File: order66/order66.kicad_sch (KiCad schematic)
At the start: 146 parts, among them J1 NICEVIEW, J2 Pouch Battery Connector, J3 swd connector, J6 millmax connector, SW1 AUX1, SW10 Z, SW11 AUX7, SW12 2, SW13 W, SW14 S, SW15 X, SW16 LALT, SW17 3, SW18 E, SW19 D, SW2 ESC, SW20 C, SW21 GUI, SW22 4, SW23 R, SW24 F, SW25 V, SW26 RAISE, SW27 5, SW28 T, SW29 G, SW3 TAB, SW30 B, SW31 LSPACE, SW32 AUX2, SW33 6, SW34 Y, SW35 H, SW36 N, SW37 RSPACE, SW38 AUX3, SW39 7, SW4 CAPSLCK, SW40 U, SW41 J, SW42 M, SW43 LOWER, SW44 AUX4, SW45 8, SW46 I, SW47 K, SW48 ,<, SW49 LEFT, SW5 LSHIFT, SW50 9, SW51 O, SW52 L, SW53 .>, SW54 DOWN, SW55 AUX5, SW56 0, SW57 P, SW58 ;:, SW59 /?, SW6 LCTRL, SW60 UP, SW61 AUX6, SW62 BACKSPACE, SW63 BACKSLACH, SW64 ENTER, SW65 RSHIFT, SW66 RIGHT, SW67 RST, SW68 ON/OFF, SW7 1, SW8 Q, SW9 A, U1 NiceNano

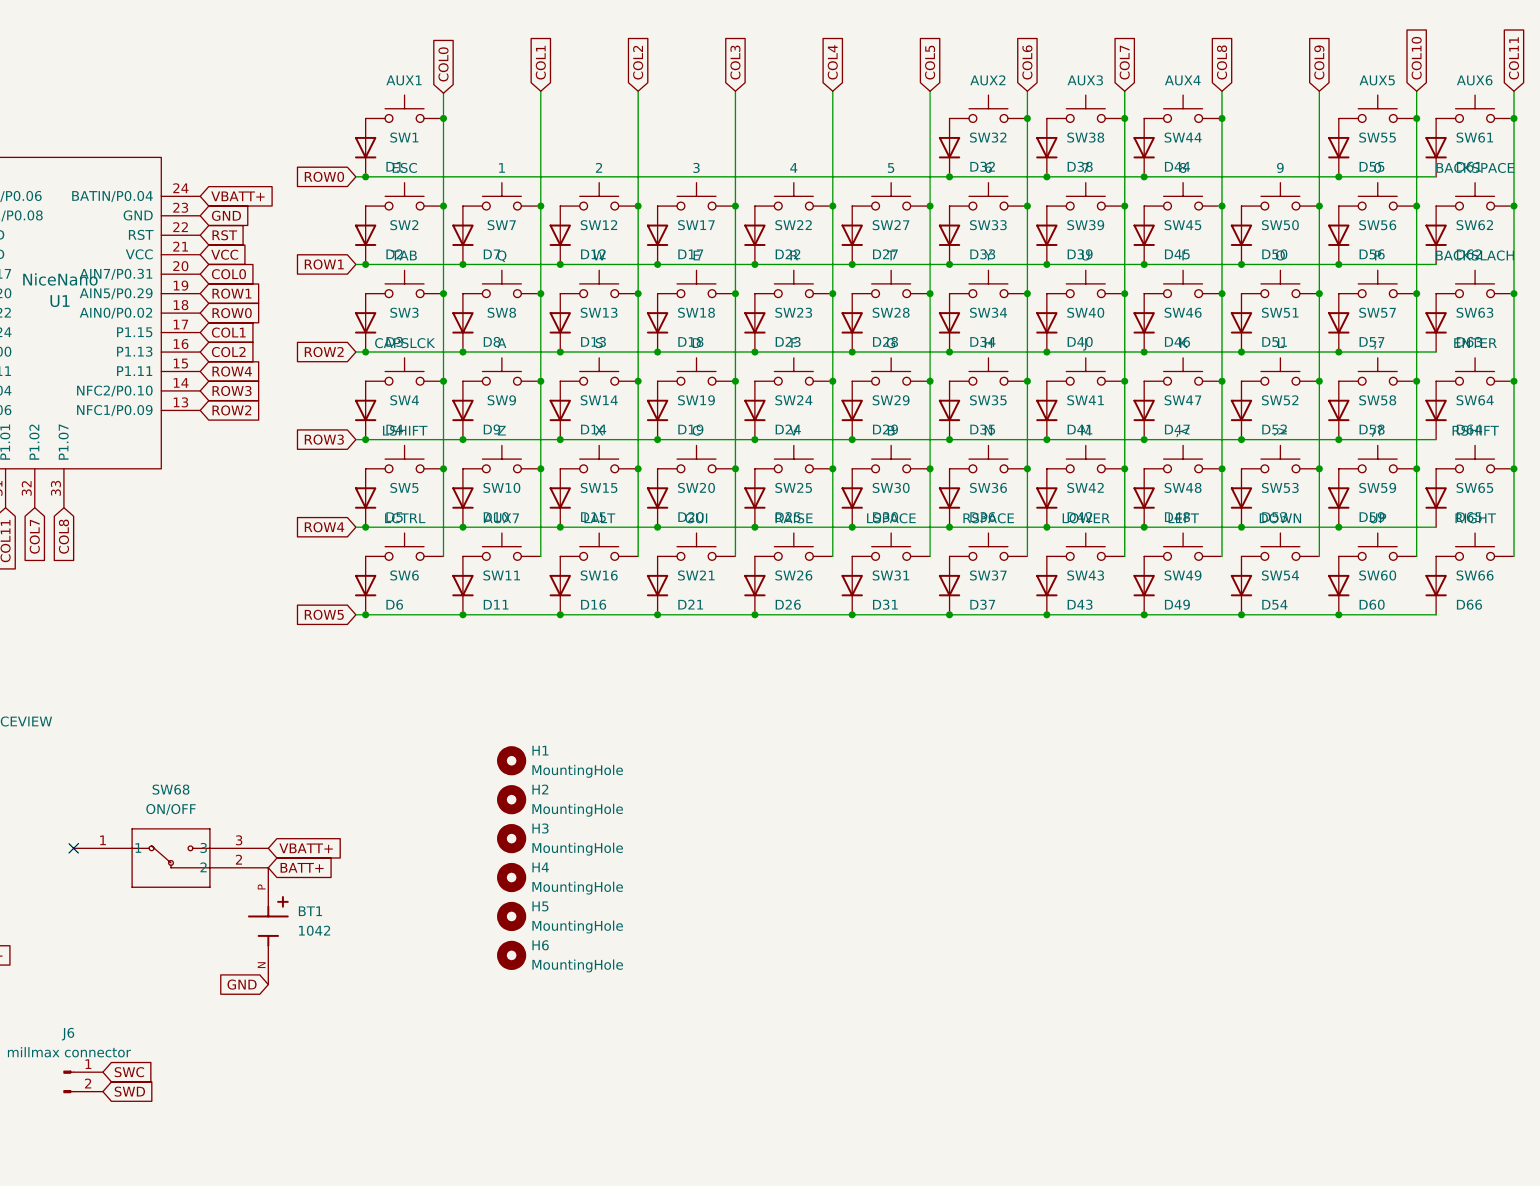
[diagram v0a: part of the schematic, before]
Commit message: Trying smd and through hole diodes same time (#2)
* added the smd sod 123 package diode symbols. havent placed/routed all the footprints yet but seems to be okay. need to figure out what I want to do with the silkscreen references. probably should just place the base numbered one and dont use the other

* placed all diode footprints. need to sort out the silkscreen overlaps

* added the other version of power switch that I have as well just in case
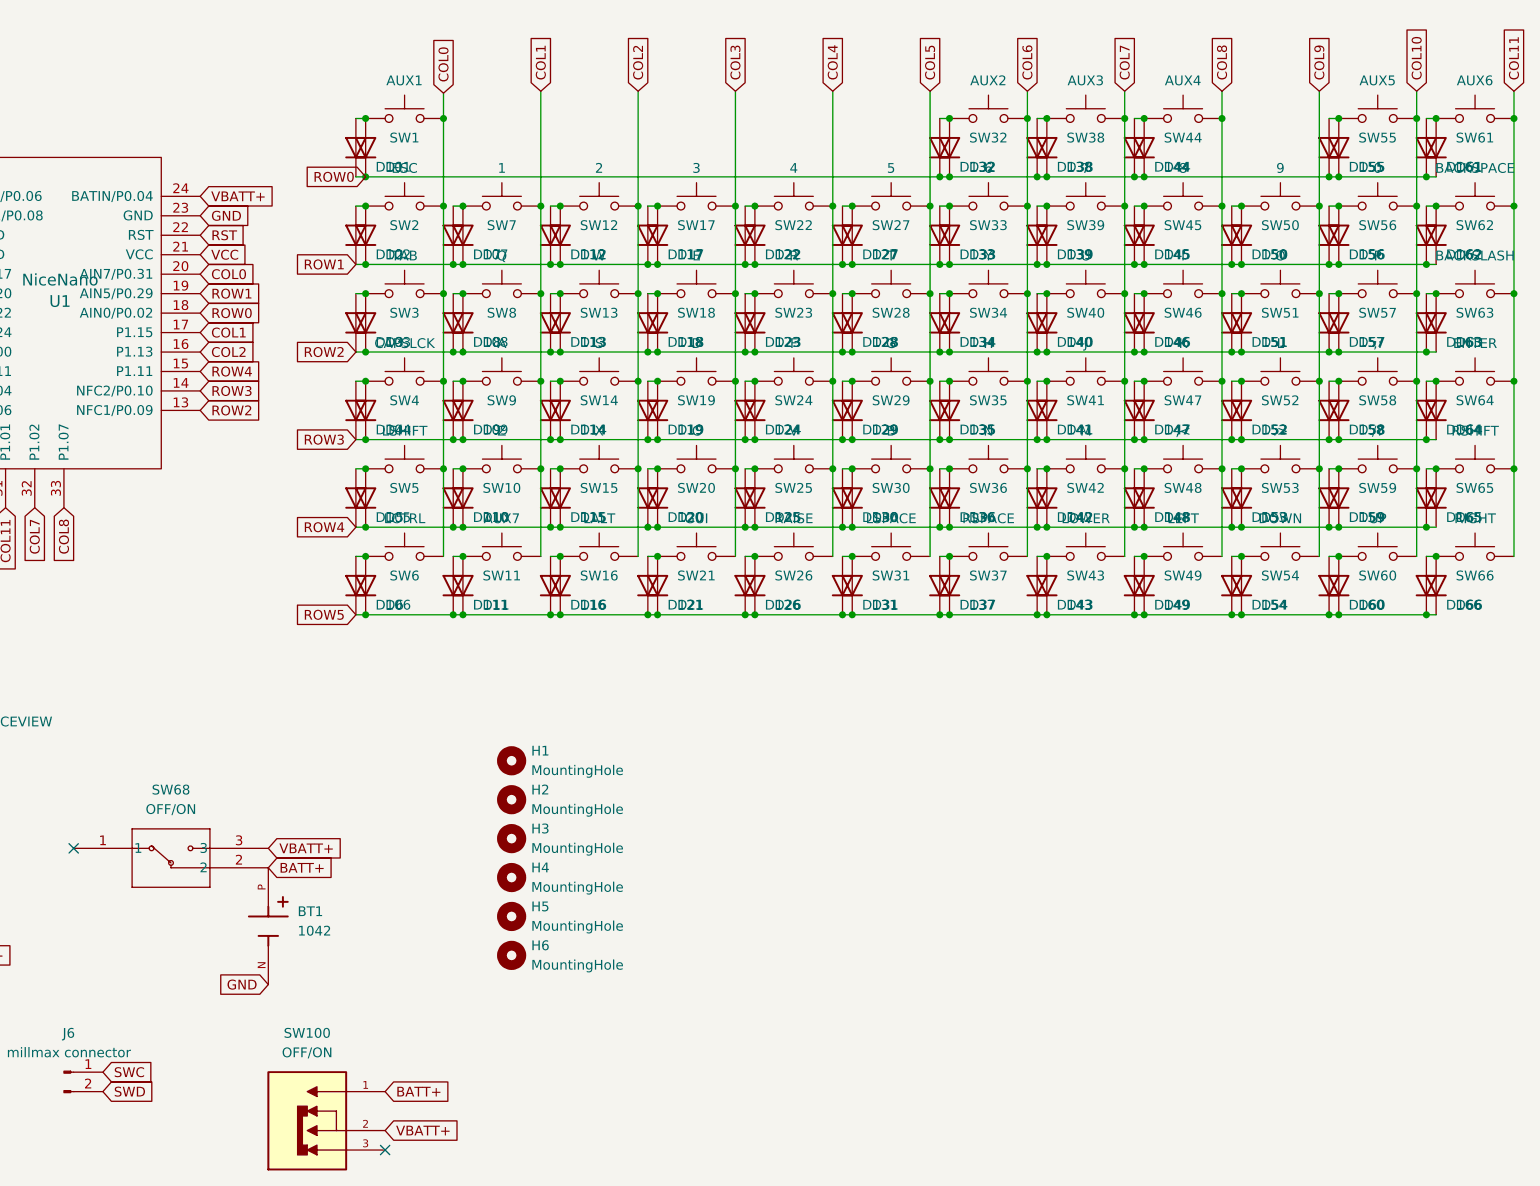
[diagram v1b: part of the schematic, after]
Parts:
- added D101, D102, D103, D104, D105, D106, D107, D108, D109, D110, D111, D112, D113, D114, D115, D116, D117, D118, D119, D120, D121, D122, D123, D124, D125, D126, D127, D128, D129, D130, D131, D132, D133, D134, D135, D136, D137, D138, D139, D140, D141, D142, D143, D144, D145, D146, D147, D148, D149, D150, D151, D152, D153, D154, D155, D156, D157, D158, D159, D160, D161, D162, D163, D164, D165, D166: 1N4148, Diode_SMD:D_SOD-123, symbol Diode:1N4148W
- added SW100: OFF/ON, SSSS811101:SW_SSSS811101, symbol SSSS811101:SSSS811101
- J6: note (none) -> try to find part number 8212200210001101 millmax spring loa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
- SW63: value BACKSLACH -> BACKSLASH
- SW68: value ON/OFF -> OFF/ON
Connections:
- net BATT+: now also SW100.1
- net ROW0: now also D101.1 (K), D132.1 (K), D138.1 (K), D144.1 (K), D155.1 (K), D161.1 (K)
- net ROW1: now also D102.1 (K), D107.1 (K), D112.1 (K), D117.1 (K), D122.1 (K), D127.1 (K), D133.1 (K), D139.1 (K), D145.1 (K), D150.1 (K), D156.1 (K), D162.1 (K)
- net ROW2: now also D103.1 (K), D108.1 (K), D113.1 (K), D118.1 (K), D123.1 (K), D128.1 (K), D134.1 (K), D140.1 (K), D146.1 (K), D151.1 (K), D157.1 (K), D163.1 (K)
- net ROW3: now also D104.1 (K), D109.1 (K), D114.1 (K), D119.1 (K), D124.1 (K), D129.1 (K), D135.1 (K), D141.1 (K), D147.1 (K), D152.1 (K), D158.1 (K), D164.1 (K)
- net ROW4: now also D105.1 (K), D110.1 (K), D115.1 (K), D120.1 (K), D125.1 (K), D130.1 (K), D136.1 (K), D142.1 (K), D148.1 (K), D153.1 (K), D159.1 (K), D165.1 (K)
- net ROW5: now also D106.1 (K), D111.1 (K), D116.1 (K), D121.1 (K), D126.1 (K), D131.1 (K), D137.1 (K), D143.1 (K), D149.1 (K), D154.1 (K), D160.1 (K), D166.1 (K)
- net VBATT+: now also SW100.2
- net at D51.2 (A), SW51.1: now also D151.2 (A)
- net at D54.2 (A), SW54.1: now also D154.2 (A)
- net at D16.2 (A), SW16.1: now also D116.2 (A)
- net at D42.2 (A), SW42.1: now also D142.2 (A)
- net at D24.2 (A), SW24.1: now also D124.2 (A)
- net at D19.2 (A), SW19.1: now also D119.2 (A)
- net at D8.2 (A), SW8.1: now also D108.2 (A)
- net at D10.2 (A), SW10.1: now also D110.2 (A)
- net at D66.2 (A), SW66.1: now also D166.2 (A)
- net at D23.2 (A), SW23.1: now also D123.2 (A)
- net at D50.2 (A), SW50.1: now also D150.2 (A)
- net at D5.2 (A), SW5.1: now also D105.2 (A)
- net at D39.2 (A), SW39.1: now also D139.2 (A)
- net at D38.2 (A), SW38.1: now also D138.2 (A)
- net at D2.2 (A), SW2.1: now also D102.2 (A)
- net at D48.2 (A), SW48.1: now also D148.2 (A)
- net at D33.2 (A), SW33.1: now also D133.2 (A)
- net at D57.2 (A), SW57.1: now also D157.2 (A)
- net at D59.2 (A), SW59.1: now also D159.2 (A)
- net at D9.2 (A), SW9.1: now also D109.2 (A)
- net at D62.2 (A), SW62.1: now also D162.2 (A)
- net at D17.2 (A), SW17.1: now also D117.2 (A)
- net at D56.2 (A), SW56.1: now also D156.2 (A)
- net at D64.2 (A), SW64.1: now also D164.2 (A)
- net at D6.2 (A), SW6.1: now also D106.2 (A)
- net at D58.2 (A), SW58.1: now also D158.2 (A)
- net at D36.2 (A), SW36.1: now also D136.2 (A)
- net at D61.2 (A), SW61.1: now also D161.2 (A)
- net at D11.2 (A), SW11.1: now also D111.2 (A)
- net at D41.2 (A), SW41.1: now also D141.2 (A)
- net at D44.2 (A), SW44.1: now also D144.2 (A)
- net at D46.2 (A), SW46.1: now also D146.2 (A)
- net at D60.2 (A), SW60.1: now also D160.2 (A)
- net at D15.2 (A), SW15.1: now also D115.2 (A)
- net at D4.2 (A), SW4.1: now also D104.2 (A)
- net at D55.2 (A), SW55.1: now also D155.2 (A)
- net at D13.2 (A), SW13.1: now also D113.2 (A)
- net at D37.2 (A), SW37.1: now also D137.2 (A)
- net at D12.2 (A), SW12.1: now also D112.2 (A)
- net at D65.2 (A), SW65.1: now also D165.2 (A)
- net at D18.2 (A), SW18.1: now also D118.2 (A)
- net at D47.2 (A), SW47.1: now also D147.2 (A)
- net at D43.2 (A), SW43.1: now also D143.2 (A)
- net at D35.2 (A), SW35.1: now also D135.2 (A)
- net at D52.2 (A), SW52.1: now also D152.2 (A)
- net at D26.2 (A), SW26.1: now also D126.2 (A)
- net at D29.2 (A), SW29.1: now also D129.2 (A)
- net at D34.2 (A), SW34.1: now also D134.2 (A)
- net at D49.2 (A), SW49.1: now also D149.2 (A)
- net at D31.2 (A), SW31.1: now also D131.2 (A)
- net at D45.2 (A), SW45.1: now also D145.2 (A)
- net at D27.2 (A), SW27.1: now also D127.2 (A)
- net at D7.2 (A), SW7.1: now also D107.2 (A)
- net at D53.2 (A), SW53.1: now also D153.2 (A)
- net at D21.2 (A), SW21.1: now also D121.2 (A)
- net at D20.2 (A), SW20.1: now also D120.2 (A)
- net at D28.2 (A), SW28.1: now also D128.2 (A)
- net at D1.2 (A), SW1.1: now also D101.2 (A)
- net at D3.2 (A), SW3.1: now also D103.2 (A)
- net at D40.2 (A), SW40.1: now also D140.2 (A)
- net at D25.2 (A), SW25.1: now also D125.2 (A)
- net at D63.2 (A), SW63.1: now also D163.2 (A)
- net at D30.2 (A), SW30.1: now also D130.2 (A)
- net at D14.2 (A), SW14.1: now also D114.2 (A)
- net at D32.2 (A), SW32.1: now also D132.2 (A)
- net at D22.2 (A), SW22.1: now also D122.2 (A)
- no-connect marks 1 -> 2

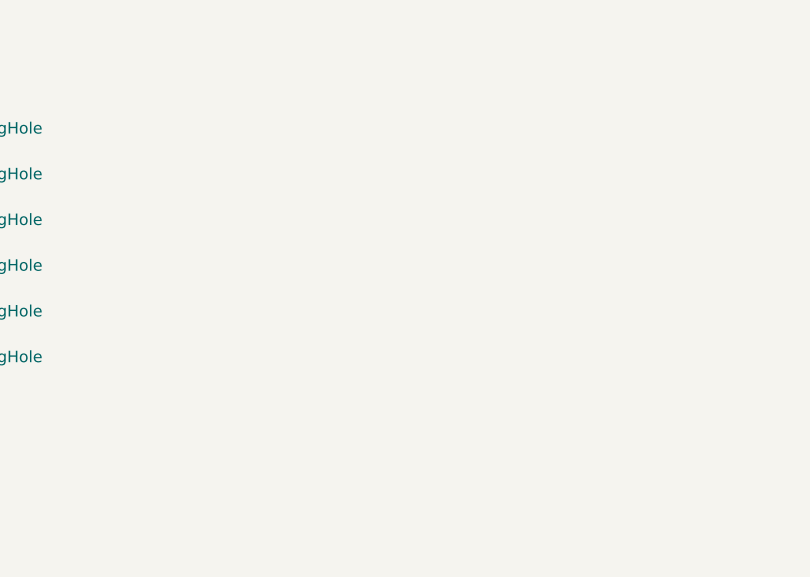
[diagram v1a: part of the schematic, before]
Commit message: adding both an order 66 logo and a connector for the jlink but that needs work
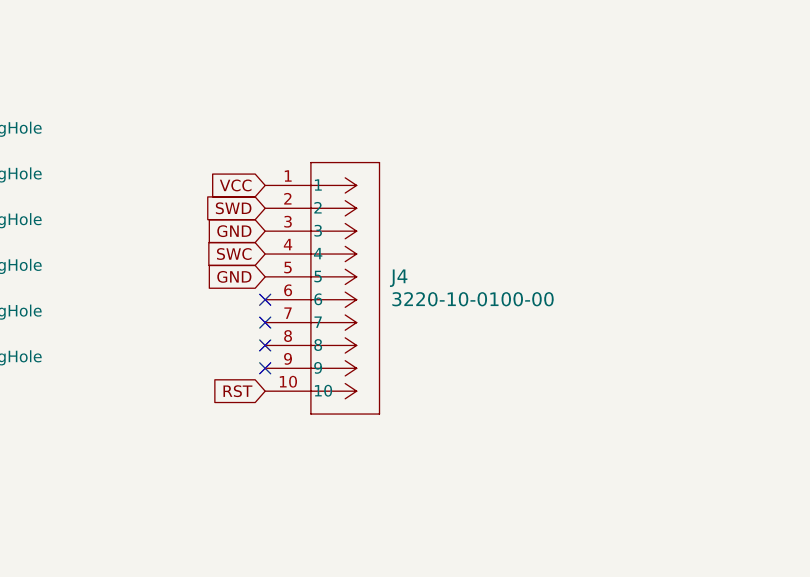
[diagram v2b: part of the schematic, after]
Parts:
- added J4: 3220-10-0100-00, 3220_10_0100_00:CONN_3220-10-0100-00_CNC, symbol 2025-06-30_18-11-54:3220-10-0100-00
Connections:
- net GND: now also J4.3, J4.5
- net RST: now also J4.10
- net SWC: now also J4.4
- net SWD: now also J4.2
- net VCC: now also J4.1
- no-connect marks 2 -> 6
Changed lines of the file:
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@@
 	)
 	(no_connect
+		(at 152.4 158.75)
+	)
+	(no_connect
+		(at 152.4 156.21)
+	)
+	(no_connect
+		(at 152.4 161.29)
+	)
+	(no_connect
 		(at 55.88 144.78)
 	)
@@
 		(at 96.52 184.15)
 	)
+	(no_connect
+		(at 152.4 153.67)
+	)
 	(wire
 		(pts
@@
 		)
 	)
+	(global_label "SWD"
+		(shape input)
+		(at 152.4 143.51 180)
+		(fields_autoplaced yes)
+		(effects
+			(font
+				(size 1.27 1.27)
+			)
+			(justify right)
+		)
+		(property "Intersheetrefs" "${INTERSHEET_REFS}"
+			(at 145.4839 143.51 0)
+			(effects
+				(font
+					(size 1.27 1.27)
+				)
+				(justify right)
+				(hide yes)
+			)
+		)
+	)
+	(global_label "SWC"
+		(shape input)
+		(at 152.4 148.59 180)
+		(fields_autoplaced yes)
+		(effects
+			(font
+				(size 1.27 1.27)
+			)
+			(justify right)
+		)
+		(property "Intersheetrefs" "${INTERSHEET_REFS}"
+			(at 145.4839 148.59 0)
+			(effects
+				(font
+					(size 1.27 1.27)
+				)
+				(justify right)
+				(hide yes)
+			)
+		)
+	)
 	(global_label "COL10"
 		(shape input)
@@
 		)
 	)
+	(global_label "GND"
+		(shape input)
+		(at 152.4 146.05 180)
+		(fields_autoplaced yes)
+		(effects
+			(font
+				(size 1.27 1.27)
+			)
+			(justify right)
+		)
+		(property "Intersheetrefs" "${INTERSHEET_REFS}"
+			(at 145.5443 146.05 0)
+			(effects
+				(font
+					(size 1.27 1.27)
+				)
+				(justify right)
+				(hide yes)
+			)
+		)
+	)
 	(global_label "COL4"
 		(shape input)
@@
 		)
 	)
+	(global_label "GND"
+		(shape input)
+		(at 152.4 151.13 180)
+		(fields_autoplaced yes)
+		(effects
+			(font
+				(size 1.27 1.27)
+			)
+			(justify right)
+		)
+		(property "Intersheetrefs" "${INTERSHEET_REFS}"
+			(at 145.5443 151.13 0)
+			(effects
+				(font
+					(size 1.27 1.27)
+				)
+				(justify right)
+				(hide yes)
+			)
+		)
+	)
 	(global_label "VBATT+"
 		(shape input)
@@
 		)
 	)
+	(global_label "RST"
+		(shape input)
+		(at 152.4 163.83 180)
+		(fields_autoplaced yes)
+		(effects
+			(font
+				(size 1.27 1.27)
+			)
+			(justify right)
+		)
+		(property "Intersheetrefs" "${INTERSHEET_REFS}"
+			(at 145.9677 163.83 0)
+			(effects
+				(font
+					(size 1.27 1.27)
+				)
+				(justify right)
+				(hide yes)
+			)
+		)
+	)
 	(global_label "ROW0"
 		(shape input)
@@
 		)
 	)
+	(global_label "VCC"
+		(shape input)
+		(at 152.4 140.97 180)
+		(fields_autoplaced yes)
+		(effects
+			(font
+				(size 1.27 1.27)
+			)
+			(justify right)
+		)
+		(property "Intersheetrefs" "${INTERSHEET_REFS}"
+			(at 145.7862 140.97 0)
+			(effects
+				(font
+					(size 1.27 1.27)
+				)
+				(justify right)
+				(hide yes)
+			)
+		)
+	)
 	(symbol
 		(lib_id "Diode:1N4148W")
@@
 					(unit 1)
 				)
+			)
+		)
+	)
+	(symbol
+		(lib_id "2025-06-30_18-11-54:3220-10-0100-00")
+		(at 152.4 140.97 0)
+		(unit 1)
+		(exclude_from_sim no)
+		(in_bom yes)
+		(on_board yes)
+		(dnp no)
+		(property "Reference" "J4"
+			(at 166.37 151.1299 0)
+			(effects
+				(font
+					(size 1.524 1.524)
+				)
+				(justify left)
+			)
+		)
+		(property "Value" "3220-10-0100-00"
+			(at 166.37 153.6699 0)
+			(effects
+				(font
+					(size 1.524 1.524)
+				)
+				(justify left)
+			)
+		)
+		(property "Footprint" "3220_10_0100_00:CONN_3220-10-0100-00_CNC"
+			(at 152.4 140.97 0)
+			(effects
+				(font
+					(size 1.27 1.27)
+					(italic yes)
+				)
+				(hide yes)
+			)
+		)
+		(property "Datasheet" "3220-10-0100-00"
+			(at 152.4 140.97 0)
+			(effects
+				(font
+					(size 1.27 1.27)
+					(italic yes)
+				)
+				(hide yes)
+			)
+		)
+		(property "Description" ""
+			(at 152.4 140.97 0)
+			(effects
+				(font
+					(size 1.27 1.27)
+				)
+				(hide yes)
+			)
+		)
+		(pin "10"
+		)
+		(pin "6"
+		)
+		(pin "5"
+		)
+		(pin "4"
+		)
+		(pin "2"
+		)
+		(pin "9"
+		)
+		(pin "8"
+		)
+		(pin "7"
+		)
+		(pin "1"
+		)
+		(pin "3"
+		)
+		(instances
+			(project ""
+				(path "/4342f055-467b-4789-a8ed-b19f1b214d4d"
+					(reference "J4")
+					(unit 1)
+				)
